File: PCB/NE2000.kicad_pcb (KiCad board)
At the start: 2 copper layers, 156.8 x 78.5 mm, 78 parts, among them J1 Bus_ISA_16bit, J2 RJ45, J3 BNC, Q1 PMBT2222, SW1 I/O addr, SW2 IRQ, SW3 Medium, SW4 ROM cfg, SW5 PNP, U1 RTL8019AS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

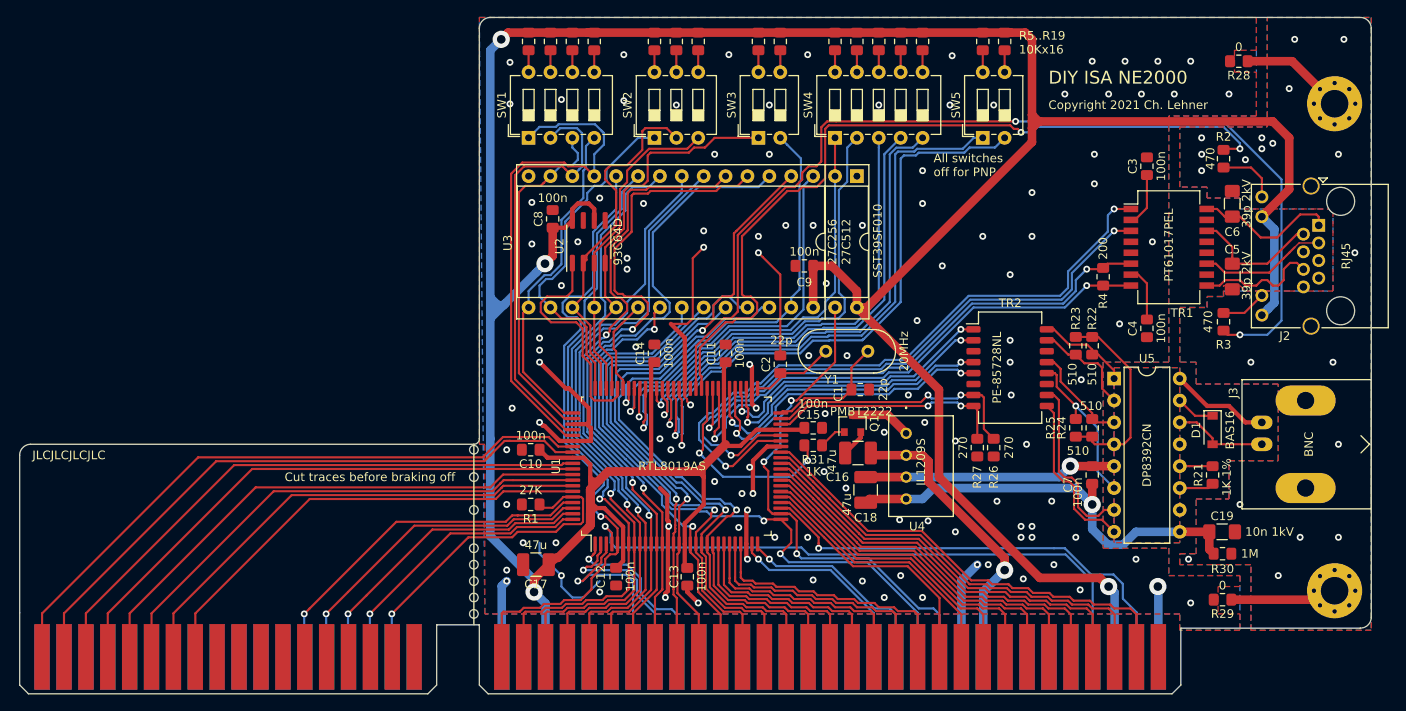
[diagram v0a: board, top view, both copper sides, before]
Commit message: Use different DC/DC converter
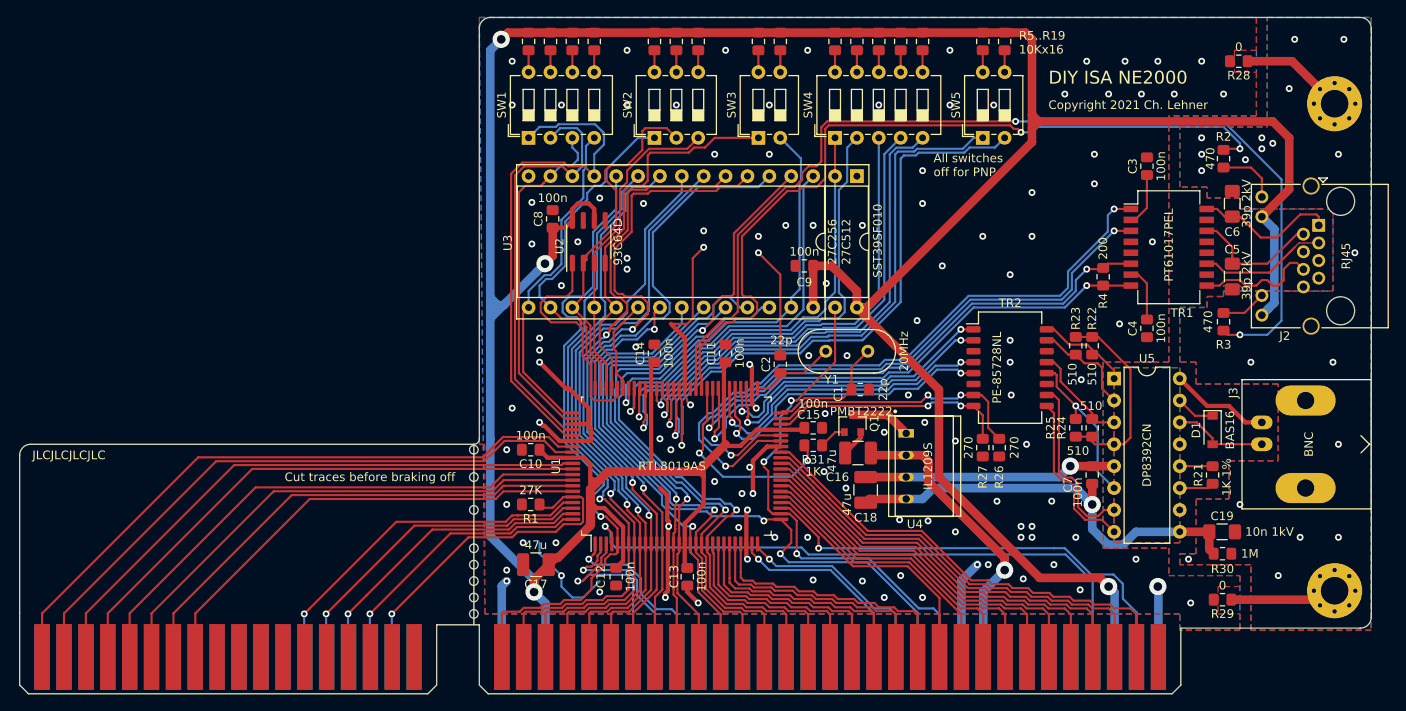
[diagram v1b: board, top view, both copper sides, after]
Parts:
- U4: footprint Samac:IL1209S -> Samac:DC_DC_12to9
- moved R26 0.63 mm to (177.2, 99.5)
- moved R27 0.63 mm to (175.3, 99.5)

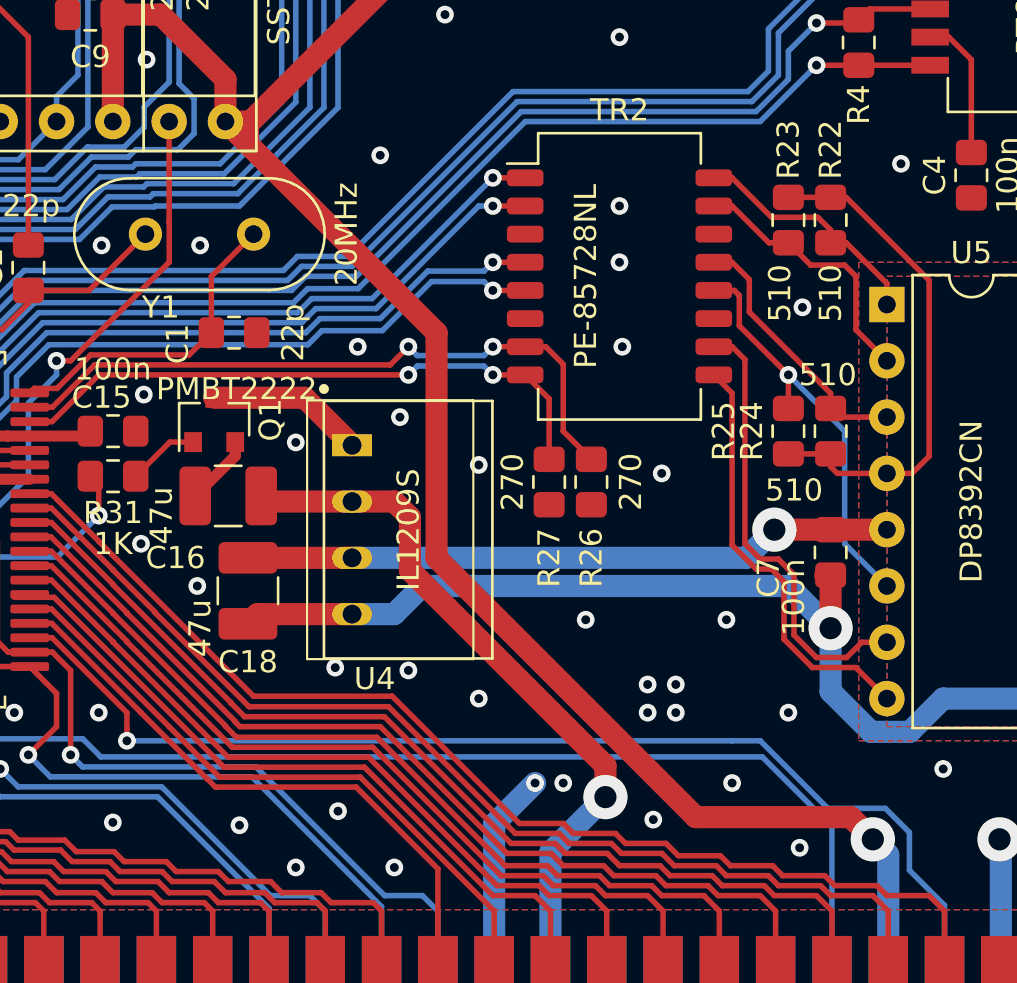
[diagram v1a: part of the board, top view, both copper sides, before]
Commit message: Moved C16 and Q1 for better soldering
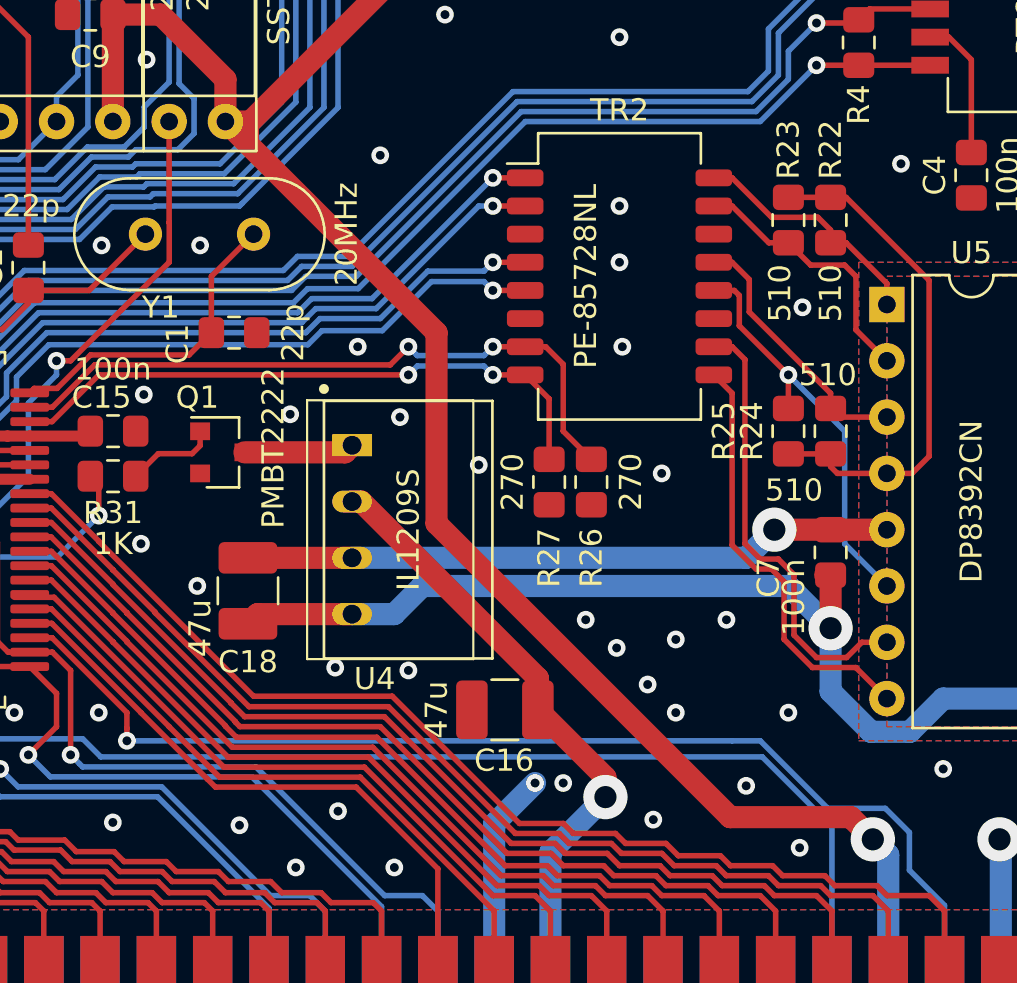
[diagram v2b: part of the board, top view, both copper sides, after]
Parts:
- moved C16 15.8 mm to (173.3, 109.7)
- moved Q1 1.51 mm to (160.5, 98.1), turned to 0 degrees
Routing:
- net +12V: track 34.5 -> 29.4 mm
- net GND: track 134.8 -> 131.6 mm, vias 120 -> 119
- net Net-(Q1-Pad3): track 7.11 -> 4.99 mm
- net +5V: track 447.9 -> 447.0 mm
- net Net-(Q1-Pad1): track 3.23 -> 4.12 mm
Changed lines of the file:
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@@
     (thickness 1.6)
     (drawings 64)
-    (tracks 2088)
+    (tracks 2085)
     (zones 0)
     (modules 78)
@@
   )
   (module Package_TO_SOT_SMD:SOT-23 (layer F.Cu)
-    (at 160.147 96.647 90)
+    (at 160.512 98.11)
     (descr "SOT-23, Standard")
     (tags SOT-23)
     (attr smd)
-    (fp_text reference Q1 (at 0 2.54 90) (layer F.SilkS)
+    (fp_text reference Q1 (at -1.127 -2.479) (layer F.SilkS)
       (effects (font (size 1 1) (thickness 0.15)))
     )
-    (fp_text value PMBT2222 (at 1.397 1.016 180) (layer F.SilkS)
+    (fp_text value PMBT2222 (at 2.302 -0.193 270) (layer F.SilkS)
       (effects (font (size 1 1) (thickness 0.15)))
     )
@@
     (fp_line (start -0.15 -1.52) (end 0.7 -1.52) (layer F.Fab) (width 0.1))
     (fp_line (start -0.7 -0.95) (end -0.7 1.5) (layer F.Fab) (width 0.1))
-    (fp_text user %R (at 0 0) (layer F.Fab)
+    (fp_text user %R (at 0 0 90) (layer F.Fab)
       (effects (font (size 0.5 0.5) (thickness 0.075)))
     )
-    (pad 3 smd rect (at 1 0 90) (size 0.9 0.8) (layers F.Cu F.Paste F.Mask)
+    (pad 3 smd rect (at 1 0) (size 0.9 0.8) (layers F.Cu F.Paste F.Mask)
       (net 125 "Net-(Q1-Pad3)"))
-    (pad 2 smd rect (at -1 0.95 90) (size 0.9 0.8) (layers F.Cu F.Paste F.Mask)
+    (pad 2 smd rect (at -1 0.95) (size 0.9 0.8) (layers F.Cu F.Paste F.Mask)
       (net 1 GND))
-    (pad 1 smd rect (at -1 -0.95 90) (size 0.9 0.8) (layers F.Cu F.Paste F.Mask)
+    (pad 1 smd rect (at -1 -0.95) (size 0.9 0.8) (layers F.Cu F.Paste F.Mask)
       (net 126 "Net-(Q1-Pad1)"))
     (model ${KISYS3DMOD}/Package_TO_SOT_SMD.3dshapes/SOT-23.wrl
@@
   )
   (module Capacitor_SMD:C_1210_3225Metric_Pad1.42x2.65mm_HandSolder (layer F.Cu)
-    (at 160.782 100.076 180)
+    (at 173.2645 109.728 180)
     (descr "Capacitor SMD 1210 (3225 Metric), square (rectangular) end terminal, IPC_7351 nominal with elongated pad for handsoldering. (Body size source: http://www.tortai-tech.com/upload/download/2011102023233369053.pdf), generated with kicad-footprint-generator")
     (tags "capacitor handsolder")
     (attr smd)
-    (fp_text reference C16 (at 2.3765 -2.794) (layer F.SilkS)
+    (fp_text reference C16 (at 0.0365 -2.286) (layer F.SilkS)
       (effects (font (size 1 1) (thickness 0.15)))
     )
-    (fp_text value 47u (at 3.0115 -0.889 90) (layer F.SilkS)
+    (fp_text value 47u (at 3.0845 0 90) (layer F.SilkS)
       (effects (font (size 1 1) (thickness 0.15)))
     )
@@
   (gr_line (start 219.075 120.396) (end 198.247 120.396) (layer Edge.Cuts) (width 0.05))
   (gr_line (start 63.5 118.618) (end 63.5 100.33) (layer Edge.Cuts) (width 0.05))
-  (via (at 163.83 97.663) (size 0.8) (drill 0.4) (layers F.Cu B.Cu) (net 1))
+  (via (at 163.576 96.393) (size 0.8) (drill 0.4) (layers F.Cu B.Cu) (net 1))
   (via (at 156.972 95.504) (size 0.8) (drill 0.4) (layers F.Cu B.Cu) (net 1))
   (via (at 156.845 102.235) (size 0.8) (drill 0.4) (layers F.Cu B.Cu) (net 1))
@@
   (segment (start 172.78 114.875) (end 174.625 113.03) (width 1) (layer B.Cu) (net 1))
   (segment (start 172.78 123.74) (end 172.78 114.875) (width 1) (layer B.Cu) (net 1))
-  (via (at 179.705 109.855) (size 0.8) (drill 0.4) (layers F.Cu B.Cu) (net 1))
+  (via (at 178.308 106.934) (size 0.8) (drill 0.4) (layers F.Cu B.Cu) (net 1))
   (via (at 180.975 109.855) (size 0.8) (drill 0.4) (layers F.Cu B.Cu) (net 1))
-  (via (at 180.975 108.585) (size 0.8) (drill 0.4) (layers F.Cu B.Cu) (net 1))
+  (via (at 180.975 106.553) (size 0.8) (drill 0.4) (layers F.Cu B.Cu) (net 1))
   (via (at 179.705 108.585) (size 0.8) (drill 0.4) (layers F.Cu B.Cu) (net 1))
   (via (at 126.365 80.645) (size 0.8) (drill 0.4) (layers F.Cu B.Cu) (net 1))
   (via (at 133.985 78.74) (size 0.8) (drill 0.4) (layers F.Cu B.Cu) (net 1))
   (via (at 133.985 77.47) (size 0.8) (drill 0.4) (layers F.Cu B.Cu) (net 1))
-  (via (at 183.515 113.03) (size 0.8) (drill 0.4) (layers F.Cu B.Cu) (net 1))
+  (via (at 184.15 113.157) (size 0.8) (drill 0.4) (layers F.Cu B.Cu) (net 1))
   (via (at 128.27 75.565) (size 0.8) (drill 0.4) (layers F.Cu B.Cu) (net 1))
   (via (at 148.971 94.869) (size 0.8) (drill 0.4) (layers F.Cu B.Cu) (net 1))
@@
   (segment (start 195.64 115.63) (end 195.58 115.57) (width 1) (layer B.Cu) (net 1))
   (segment (start 195.64 123.74) (end 195.64 115.63) (width 1) (layer B.Cu) (net 1))
-  (via (at 172.085 109.22) (size 0.8) (drill 0.4) (layers F.Cu B.Cu) (net 1))
   (via (at 187.325 54.61) (size 0.8) (drill 0.4) (layers F.Cu B.Cu) (net 1))
   (via (at 191.77 54.61) (size 0.8) (drill 0.4) (layers F.Cu B.Cu) (net 1))
@@
   (via (at 122.936 75.819) (size 0.8) (drill 0.4) (layers F.Cu B.Cu) (net 1))
   (via (at 167.64 84.709) (size 0.8) (drill 0.4) (layers F.Cu B.Cu) (net 1))
-  (segment (start 161.097 98.2735) (end 159.2945 100.076) (width 0.5) (layer F.Cu) (net 1))
-  (segment (start 161.097 97.647) (end 161.097 98.2735) (width 0.5) (layer F.Cu) (net 1))
   (segment (start 160.02 90.17) (end 161.925 88.265) (width 0.25) (layer F.Cu) (net 2))
   (segment (start 160.02 92.71) (end 160.02 90.17) (width 0.25) (layer F.Cu) (net 2))
@@
   (segment (start 208.398999 83.330001) (end 207.649 84.08) (width 1) (layer B.Cu) (net 17))
   (segment (start 207.649 72.65) (end 209.099001 74.100001) (width 1) (layer B.Cu) (net 17))
-  (segment (start 188.865001 114.570001) (end 189.865 115.57) (width 1) (layer F.Cu) (net 17))
-  (segment (start 170.18 102.87) (end 181.880001 114.570001) (width 1) (layer F.Cu) (net 17))
-  (segment (start 170.18 92.71) (end 170.18 102.87) (width 1) (layer F.Cu) (net 17))
-  (segment (start 181.880001 114.570001) (end 188.865001 114.570001) (width 1) (layer F.Cu) (net 17))
   (segment (start 136.775 89.92) (end 137.16 89.535) (width 0.5) (layer F.Cu) (net 17))
   (segment (start 136.775 92.575) (end 136.775 89.92) (width 0.5) (layer F.Cu) (net 17))
@@
   (segment (start 161.671 83.30037) (end 161.78637 83.185) (width 1) (layer F.Cu) (net 17))
   (segment (start 161.671 84.201) (end 161.671 83.30037) (width 1) (layer F.Cu) (net 17))
-  (segment (start 161.671 84.201) (end 170.18 92.71) (width 1) (layer F.Cu) (net 17))
   (segment (start 160.655 83.185) (end 161.671 84.201) (width 1) (layer F.Cu) (net 17))
   (segment (start 155.575 78.368) (end 155.584 78.359) (width 1) (layer F.Cu) (net 17))
@@
   (segment (start 126.793 73.932) (end 127.635 73.09) (width 0.5) (layer F.Cu) (net 17))
   (segment (start 125.349 73.932) (end 126.793 73.932) (width 0.5) (layer F.Cu) (net 17))
+  (segment (start 170.18 92.71) (end 161.671 84.201) (width 1) (layer F.Cu) (net 17))
+  (segment (start 170.18 101.323002) (end 170.18 92.71) (width 1) (layer F.Cu) (net 17))
+  (segment (start 183.426999 114.570001) (end 170.18 101.323002) (width 1) (layer F.Cu) (net 17))
+  (segment (start 188.865001 114.570001) (end 183.426999 114.570001) (width 1) (layer F.Cu) (net 17))
+  (segment (start 189.865 115.57) (end 188.865001 114.570001) (width 1) (layer F.Cu) (net 17))
   (via (at 96.52 118.745) (size 0.8) (drill 0.4) (layers F.Cu B.Cu) (net 18))
   (segment (start 96.52 123.68) (end 96.58 123.74) (width 0.25) (layer B.Cu) (net 18))
@@
   (segment (start 175.32 123.74) (end 175.32 116.145) (width 1) (layer B.Cu) (net 105))
   (via (at 177.8 113.665) (size 2) (drill 1) (layers F.Cu B.Cu) (net 105))
-  (segment (start 168.97999 103.430777) (end 177.8 112.250787) (width 1) (layer F.Cu) (net 105))
-  (segment (start 168.97999 101.03999) (end 168.97999 103.430777) (width 1) (layer F.Cu) (net 105))
-  (segment (start 177.8 112.250787) (end 177.8 113.665) (width 1) (layer F.Cu) (net 105))
-  (segment (start 168.27 100.33) (end 168.97999 101.03999) (width 1) (layer F.Cu) (net 105))
-  (segment (start 166.37 100.33) (end 168.27 100.33) (width 1) (layer F.Cu) (net 105))
-  (segment (start 162.5235 100.33) (end 162.2695 100.076) (width 1) (layer F.Cu) (net 105))
-  (segment (start 166.37 100.33) (end 162.5235 100.33) (width 1) (layer F.Cu) (net 105))
+  (segment (start 177.8 112.776) (end 174.752 109.728) (width 1) (layer F.Cu) (net 105))
+  (segment (start 177.8 113.665) (end 177.8 112.776) (width 1) (layer F.Cu) (net 105))
+  (segment (start 166.779 100.33) (end 166.37 100.33) (width 1) (layer F.Cu) (net 105))
+  (segment (start 174.752 108.303) (end 166.779 100.33) (width 1) (layer F.Cu) (net 105))
+  (segment (start 174.752 109.728) (end 174.752 108.303) (width 1) (layer F.Cu) (net 105))
   (segment (start 199.25137 96.52) (end 198.12 96.52) (width 0.25) (layer F.Cu) (net 106))
   (segment (start 200.09 96.52) (end 199.25137 96.52) (width 0.25) (layer F.Cu) (net 106))
@@
   (segment (start 208.28141 78.105) (end 211.70641 74.68) (width 0.25) (layer F.Cu) (net 124))
   (segment (start 204.216 78.105) (end 208.28141 78.105) (width 0.25) (layer F.Cu) (net 124))
-  (segment (start 164.227 95.647) (end 160.147 95.647) (width 1) (layer F.Cu) (net 125))
-  (segment (start 166.37 97.79) (end 164.227 95.647) (width 1) (layer F.Cu) (net 125))
-  (segment (start 158.149 97.647) (end 159.197 97.647) (width 0.25) (layer F.Cu) (net 126))
-  (segment (start 156.609 99.187) (end 158.149 97.647) (width 0.25) (layer F.Cu) (net 126))
+  (segment (start 166.05 98.11) (end 166.37 97.79) (width 1) (layer F.Cu) (net 125))
+  (segment (start 161.512 98.11) (end 166.05 98.11) (width 1) (layer F.Cu) (net 125))
+  (segment (start 159.512 97.81) (end 159.151 98.171) (width 0.25) (layer F.Cu) (net 126))
+  (segment (start 159.512 97.16) (end 159.512 97.81) (width 0.25) (layer F.Cu) (net 126))
+  (segment (start 157.625 98.171) (end 156.609 99.187) (width 0.25) (layer F.Cu) (net 126))
+  (segment (start 159.151 98.171) (end 157.625 98.171) (width 0.25) (layer F.Cu) (net 126))
   (segment (start 142.367 100.076) (end 142.367 100.076) (width 0.25) (layer F.Cu) (net 127))
   (via (at 142.367 100.076) (size 0.8) (drill 0.4) (layers F.Cu B.Cu) (net 127))
